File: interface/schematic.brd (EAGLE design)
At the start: 100 x 46 mm, 31 parts, among them J1 AUDIO_JACK_3.5MM_KIT, J2 AUDIO_JACK_3.5MM_KIT, J3 RJ45, T1 2N3904, T2 2N3904

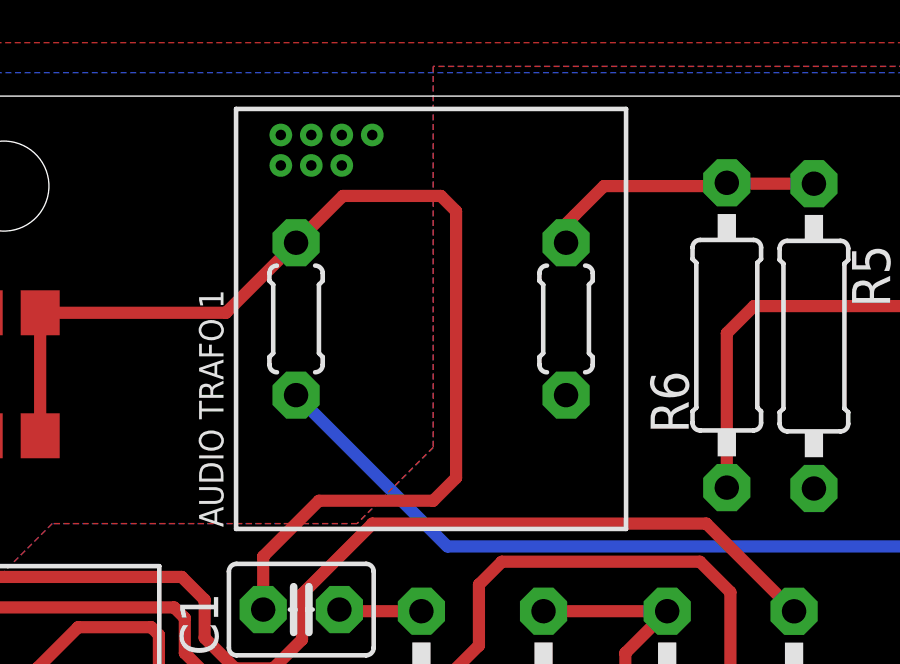
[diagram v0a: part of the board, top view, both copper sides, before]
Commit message: Fixed component numbering to match ordered boards
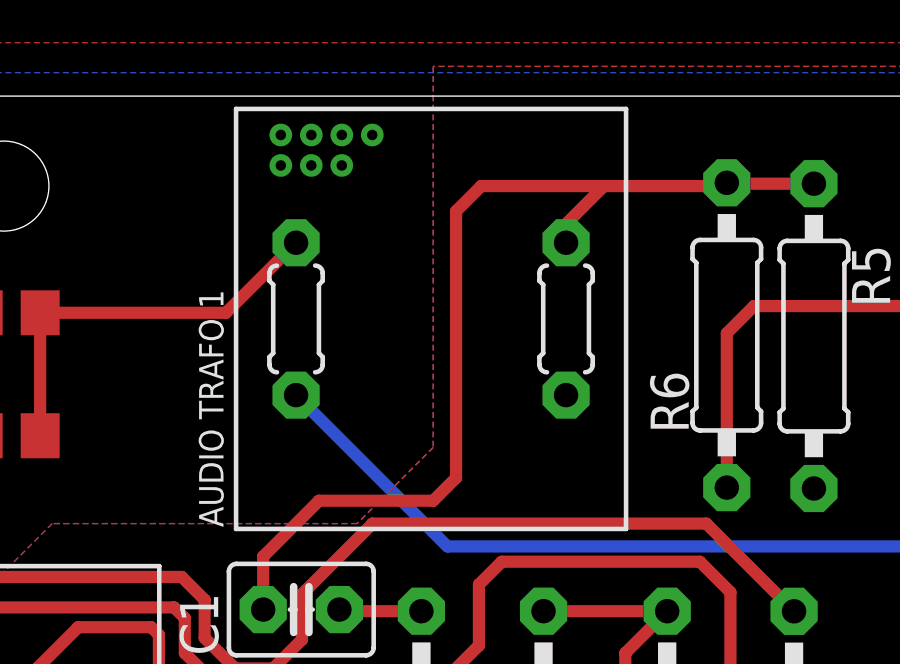
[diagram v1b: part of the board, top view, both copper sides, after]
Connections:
- removed net N$8: L2.1, R5.1, R6.2
- new net N$16: L1.1, R3.1, R4.1
- net N$15: now also L2.1, R5.1, R6.2; no longer L1.1, R3.1, R4.1
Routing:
- net N$16: track 0.00 -> 13.6 mm
- net N$8: track 9.49 -> 0.00 mm
- net N$15: track 38.0 -> 32.9 mm
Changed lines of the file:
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@@
 <via x="62.23" y="43.688" extent="1-16" drill="0.35"/>
-</signal>
-<signal name="N$8">
-<contactref element="L2" pad="1"/>
-<contactref element="R6" pad="2"/>
-<wire x1="77.096" y1="43.11" x2="77.066" y2="43.08" width="0.4064" layer="1"/>
-<wire x1="76.986" y1="43" x2="73" y2="43" width="0.4064" layer="1"/>
-<wire x1="73" y1="43" x2="72.023" y2="42.023" width="0.4064" layer="1"/>
-<contactref element="R5" pad="1"/>
-<wire x1="80" y1="43.08" x2="77.066" y2="43.08" width="0.4064" layer="1"/>
-<wire x1="77.066" y1="43.08" x2="76.986" y2="43" width="0.4064" layer="1"/>
-<wire x1="71.738" y1="41.112" x2="71.738" y2="41.738" width="0.4064" layer="1"/>
-<wire x1="71.738" y1="41.738" x2="72.023" y2="42.023" width="0.4064" layer="1"/>
 </signal>
 <signal name="RIG_MIC_IN">
@@
 </signal>
 <signal name="N$15">
-<contactref element="L1" pad="1"/>
-<contactref element="R3" pad="1"/>
-<contactref element="R4" pad="1"/>
 <contactref element="C1" pad="1"/>
-<wire x1="60.4028" y1="38.7768" x2="62.738" y2="41.112" width="0.4064" layer="1"/>
-<wire x1="54.208" y1="38.7768" x2="60.4028" y2="38.7768" width="0.4064" layer="1"/>
-<wire x1="54.208" y1="34.678" x2="54.208" y2="38.7768" width="0.4064" layer="1"/>
-<wire x1="62.738" y1="41.112" x2="64.298" y2="42.672" width="0.4064" layer="1"/>
-<wire x1="64.298" y1="42.672" x2="67.564" y2="42.672" width="0.4064" layer="1"/>
 <wire x1="61.642" y1="28.884" x2="61.642" y2="30.654" width="0.4064" layer="1"/>
 <wire x1="67.31" y1="32.512" x2="63.5" y2="32.512" width="0.4064" layer="1"/>
 <wire x1="61.642" y1="30.654" x2="63.5" y2="32.512" width="0.4064" layer="1"/>
-<wire x1="67.564" y1="42.672" x2="68.072" y2="42.164" width="0.4064" layer="1"/>
 <wire x1="68.072" y1="33.274" x2="67.31" y2="32.512" width="0.4064" layer="1"/>
-<wire x1="68.072" y1="42.164" x2="68.072" y2="33.274" width="0.4064" layer="1"/>
+<wire x1="68.072" y1="33.274" x2="68.072" y2="42.164" width="0.4064" layer="1"/>
+<contactref element="L2" pad="1"/>
+<contactref element="R6" pad="2"/>
+<contactref element="R5" pad="1"/>
+<wire x1="77.096" y1="43.11" x2="77.066" y2="43.08" width="0.4064" layer="1"/>
+<wire x1="76.986" y1="43" x2="73" y2="43" width="0.4064" layer="1"/>
+<wire x1="73" y1="43" x2="71.738" y2="41.738" width="0.4064" layer="1"/>
+<wire x1="80" y1="43.08" x2="77.066" y2="43.08" width="0.4064" layer="1"/>
+<wire x1="77.066" y1="43.08" x2="76.986" y2="43" width="0.4064" layer="1"/>
+<wire x1="71.738" y1="41.112" x2="71.738" y2="41.738" width="0.4064" layer="1"/>
+<wire x1="68.072" y1="42.164" x2="68.908" y2="43" width="0.4064" layer="1"/>
+<wire x1="68.908" y1="43" x2="73" y2="43" width="0.4064" layer="1"/>
 </signal>
 <signal name="N$5">
@@
 <wire x1="45.778" y1="14.08" x2="51.0696" y2="8.7884" width="0.4064" layer="16"/>
 </signal>
+<signal name="N$16">
+<contactref element="L1" pad="1"/>
+<contactref element="R3" pad="1"/>
+<contactref element="R4" pad="1"/>
+<wire x1="60.4028" y1="38.7768" x2="62.738" y2="41.112" width="0.4064" layer="1"/>
+<wire x1="54.208" y1="38.7768" x2="60.4028" y2="38.7768" width="0.4064" layer="1"/>
+<wire x1="54.208" y1="34.678" x2="54.208" y2="38.7768" width="0.4064" layer="1"/>
+</signal>
 </signals>
